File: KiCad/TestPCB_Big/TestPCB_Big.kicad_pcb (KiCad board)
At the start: 2 copper layers, 101.6 x 76.2 mm, 57 parts, among them J2 USB4135-GF-A, Q1 SFH_3711, Q2 2N7002, Q3 2N7002, U2 TC1185-xCT, U3 MCP73831-2-OT

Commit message: CHG: cleanub of vias
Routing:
- net Net-(U2-GND): track 82.1 -> 102.1 mm
- net Net-(U3-V_{DD}): track 26.0 -> 27.8 mm
- net Net-(D1-K): track 4.56 -> 6.13 mm

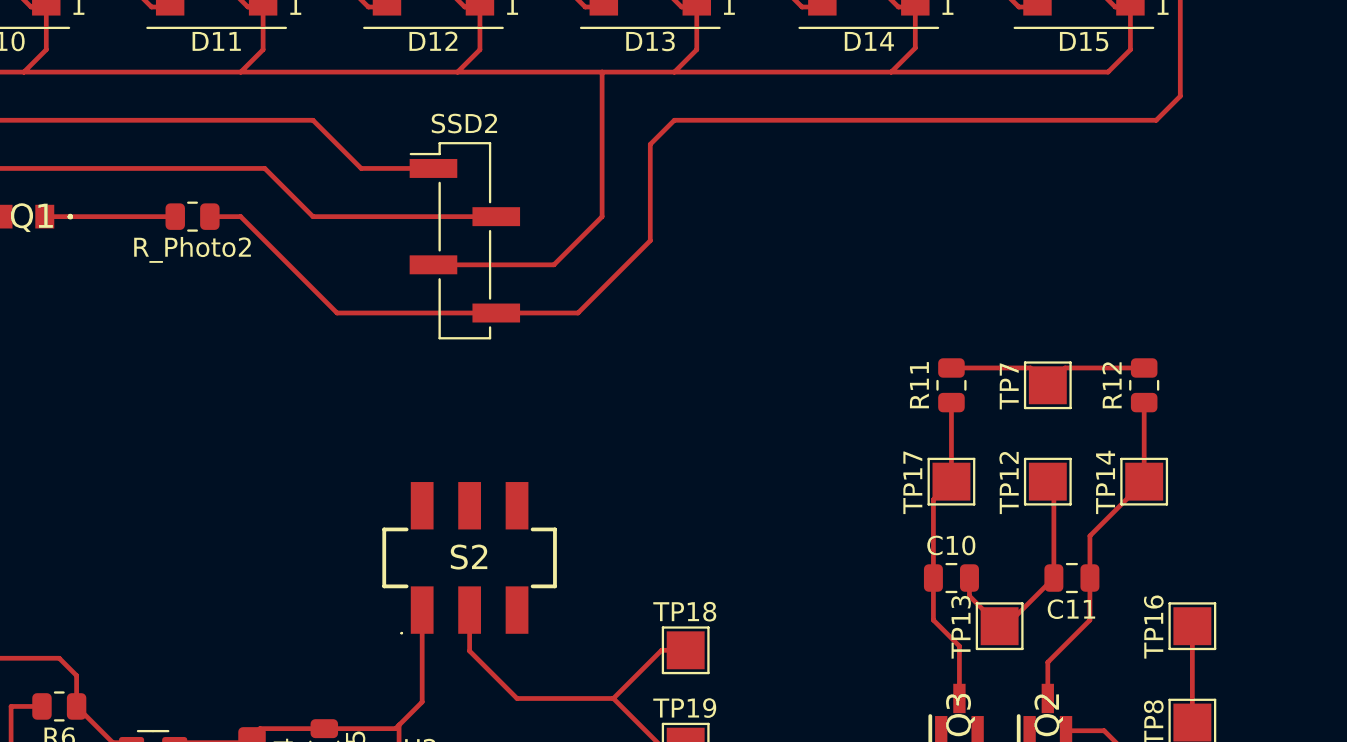
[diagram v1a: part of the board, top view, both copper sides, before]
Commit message: CHG: pcb-layouts adopted
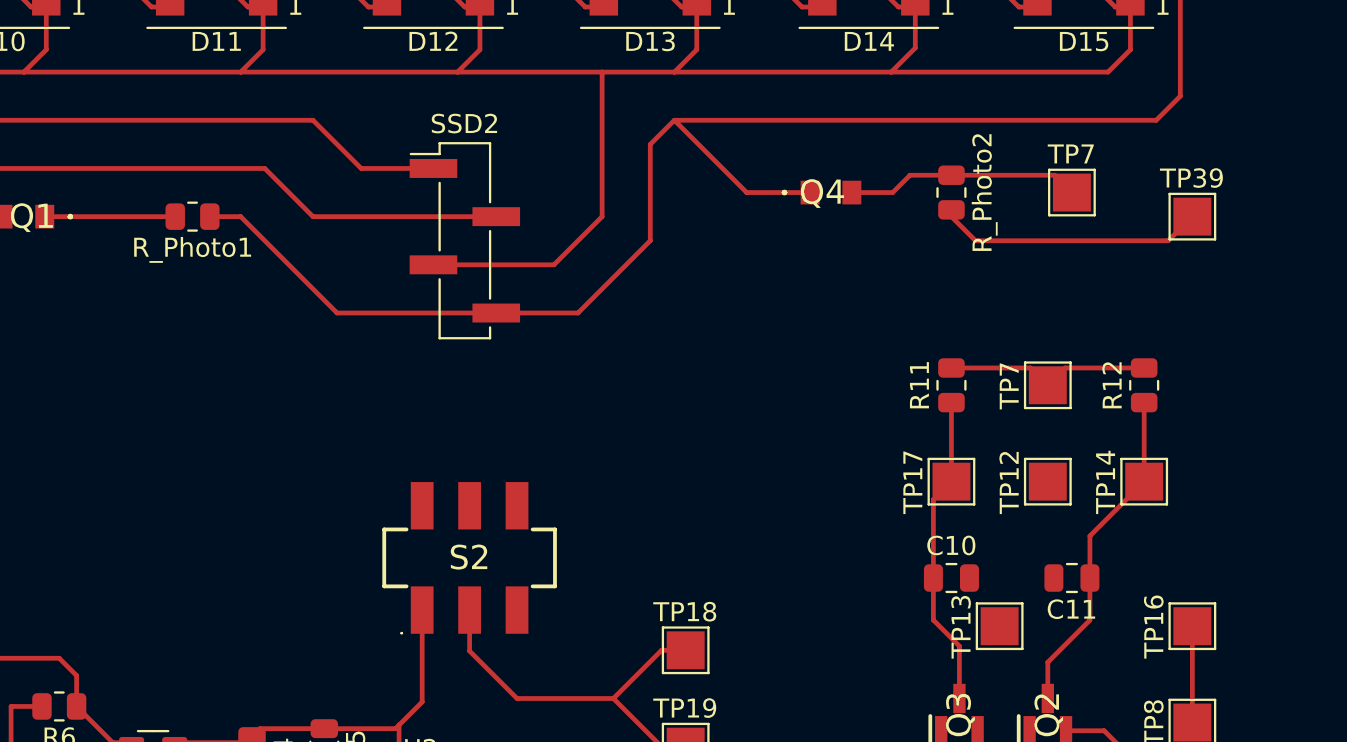
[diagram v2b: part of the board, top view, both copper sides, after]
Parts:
- added Q4: SFH_3711, SFH_3711:SFH3711, F.Cu at (120.7, 77.5)
- added R_Photo2: 10kΩ, Resistor_SMD:R_0805_2012Metric, F.Cu at (127.0, 77.5)
- added TP39: +3.3V Photo, TestPoint:TestPoint_Pad_2.0x2.0mm, F.Cu at (139.7, 78.7)
- added TP7: GPIO_Photo2, TestPoint:TestPoint_Pad_2.0x2.0mm, F.Cu at (133.3, 77.5)
- TP13: value GND -> FL_GND
- TP31: value GPIO_Photo -> GPIO_Photo1
- renumbered R_Photo2 to R_Photo1
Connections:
- TP12 pad 1: Net-(C10-Pad2) -> Net-(TP12-Pad1)
- TP13 pad 1: Net-(C10-Pad2) -> Net-(TP12-Pad1)
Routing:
- net Net-(R_Photo2-Pad2): track 0.00 -> 14.1 mm
- net Net-(Q4-C): track 0.00 -> 12.4 mm
- net Net-(C10-Pad2): track 12.3 -> 0.00 mm
- net Net-(D10-VSS): track 198.1 -> 206.8 mm

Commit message: CHG: changes of today
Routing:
- net Net-(TP12-Pad1): track 0.00 -> 8.67 mm
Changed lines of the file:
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@@
   (segment (start 127 78.74) (end 127 78.3825) (width 0.25) (layer "F.Cu") (net 41))
   (segment (start 139.7 78.74) (end 138.43 80.01) (width 0.25) (layer "F.Cu") (net 41))
+  (segment (start 132.08 92.71) (end 129.54 95.25) (width 0.25) (layer "F.Cu") (net 42))
+  (segment (start 129.54 95.25) (end 129.54 100.33) (width 0.25) (layer "F.Cu") (net 42))
 )
